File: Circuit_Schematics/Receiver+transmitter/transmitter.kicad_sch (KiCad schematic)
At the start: 21 parts, among them Q1 2N2219, Q2 2N2219, Q3 2N2219, U2 PIR, U3 PIR, U8 RF Receiver

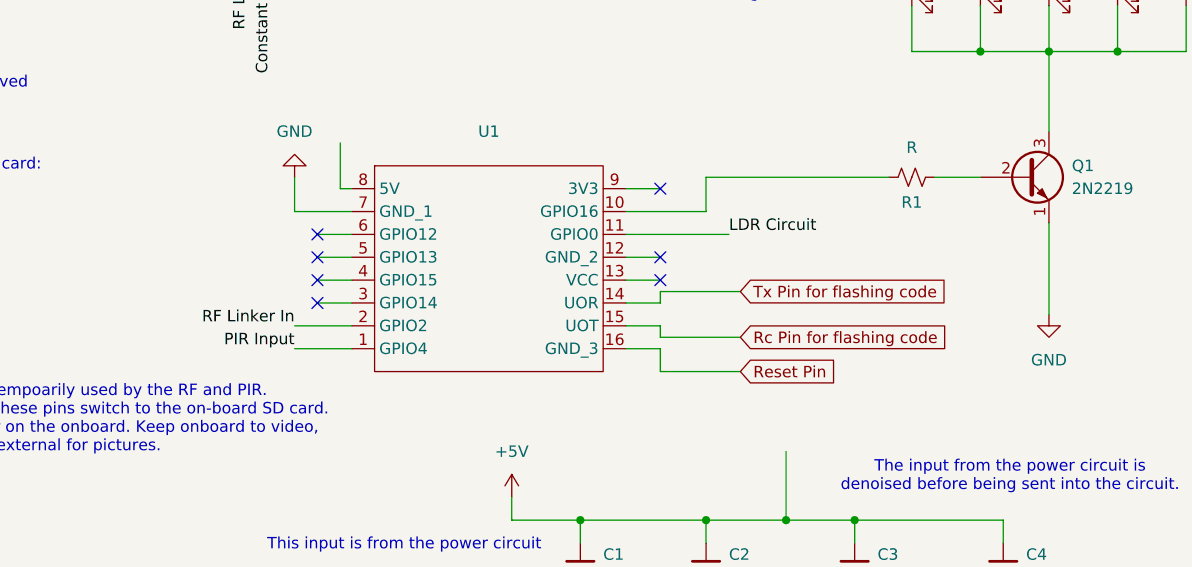
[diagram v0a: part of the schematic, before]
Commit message: Circuit schematics
Made a few additions to the circuit schematic
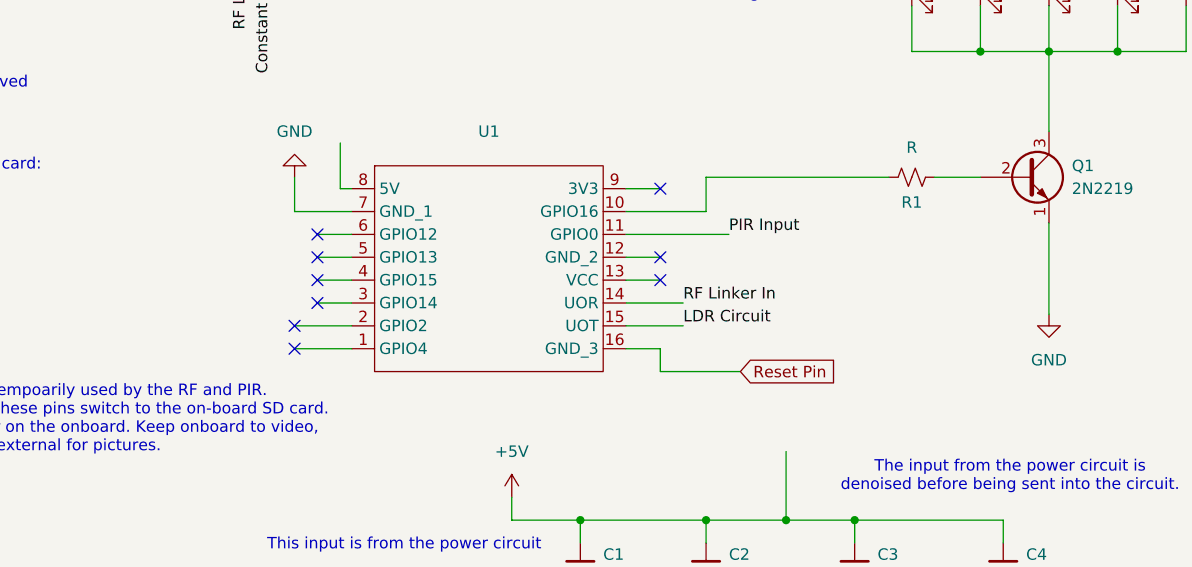
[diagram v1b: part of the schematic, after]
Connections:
- net Rc Pin for flashing code is gone; now on net LDR Circuit: U1.15 (UOT)
- net Tx Pin for flashing code is gone; now on net RF Linker In: U1.14 (UOR)
- net LDR Circuit: no longer U1.11 (GPIO0)
- net PIR Input: now also U1.11 (GPIO0); no longer U1.1 (GPIO4)
- net RF Linker In: no longer U1.2 (GPIO2)
- no-connect marks 7 -> 9
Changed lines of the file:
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@@
+	)
+	(no_connect
+		(at 76.2 91.44)
 	)
 	(no_connect
@@
 	)
 	(no_connect
+		(at 76.2 93.98)
+	)
+	(no_connect
 		(at 78.74 88.9)
 	)
@@
 	(wire
 		(pts
-			(xy 116.84 88.9) (xy 113.03 88.9)
-		)
-		(stroke
-			(width 0)
-			(type default)
-		)
-	)
-	(wire
-		(pts
 			(xy 175.26 55.88) (xy 175.26 60.96)
 		)
@@
 	(wire
 		(pts
+			(xy 113.03 91.44) (xy 119.38 91.44)
+		)
+		(stroke
+			(width 0)
+			(type default)
+		)
+	)
+	(wire
+		(pts
 			(xy 125.73 96.52) (xy 116.84 96.52)
 		)
@@
 	(wire
 		(pts
-			(xy 125.73 87.63) (xy 116.84 87.63)
-		)
-		(stroke
-			(width 0)
-			(type default)
-		)
-	)
-	(wire
-		(pts
 			(xy 116.84 96.52) (xy 116.84 93.98)
 		)
@@
 	(wire
 		(pts
-			(xy 116.84 87.63) (xy 116.84 88.9)
-		)
-		(stroke
-			(width 0)
-			(type default)
-		)
-	)
-	(wire
-		(pts
 			(xy 76.2 91.44) (xy 82.55 91.44)
 		)
@@
 	(wire
 		(pts
-			(xy 116.84 92.71) (xy 116.84 91.44)
-		)
-		(stroke
-			(width 0)
-			(type default)
-		)
-	)
-	(wire
-		(pts
 			(xy 116.84 83.82) (xy 113.03 83.82)
 		)
@@
 	(wire
 		(pts
-			(xy 125.73 92.71) (xy 116.84 92.71)
-		)
-		(stroke
-			(width 0)
-			(type default)
-		)
-	)
-	(wire
-		(pts
 			(xy 116.84 76.2) (xy 113.03 76.2)
 		)
@@
 	(wire
 		(pts
-			(xy 116.84 91.44) (xy 113.03 91.44)
-		)
-		(stroke
-			(width 0)
-			(type default)
-		)
-	)
-	(wire
-		(pts
 			(xy 175.26 48.26) (xy 175.26 39.37)
 		)
@@
 		(pts
 			(xy 160.02 60.96) (xy 167.64 60.96)
+		)
+		(stroke
+			(width 0)
+			(type default)
+		)
+	)
+	(wire
+		(pts
+			(xy 113.03 88.9) (xy 119.38 88.9)
 		)
 		(stroke
@@
 	)
 	(label "LDR Circuit"
-		(at 124.46 81.28 0)
+		(at 119.38 91.44 0)
 		(fields_autoplaced yes)
 		(effects
@@
 	)
 	(label "RF Linker In"
-		(at 76.2 91.44 180)
+		(at 119.38 88.9 0)
 		(fields_autoplaced yes)
 		(effects
@@
 				(size 1.27 1.27)
 			)
-			(justify right bottom)
+			(justify left bottom)
 		)
 	)
 	(label "PIR Input"
-		(at 76.2 93.98 180)
+		(at 124.46 81.28 0)
 		(fields_autoplaced yes)
 		(effects
@@
 				(size 1.27 1.27)
 			)
-			(justify right bottom)
-		)
-	)
-	(global_label "Tx Pin for flashing code"
-		(shape input)
-		(at 125.73 87.63 0)
-		(fields_autoplaced yes)
-		(effects
-			(font
-				(size 1.27 1.27)
-			)
-			(justify left)
-		)
-		(property "Intersheetrefs" "${INTERSHEET_REFS}"
-			(at 152.361 87.63 0)
-			(effects
-				(font
-					(size 1.27 1.27)
-				)
-				(justify left)
-				(hide yes)
-			)
-		)
-	)
-	(global_label "Rc Pin for flashing code"
-		(shape input)
-		(at 125.73 92.71 0)
-		(fields_autoplaced yes)
-		(effects
-			(font
-				(size 1.27 1.27)
-			)
-			(justify left)
-		)
-		(property "Intersheetrefs" "${INTERSHEET_REFS}"
-			(at 152.7239 92.71 0)
-			(effects
-				(font
-					(size 1.27 1.27)
-				)
-				(justify left)
-				(hide yes)
-			)
-		)
-	)
+			(justify left bottom)
+		)
+	)

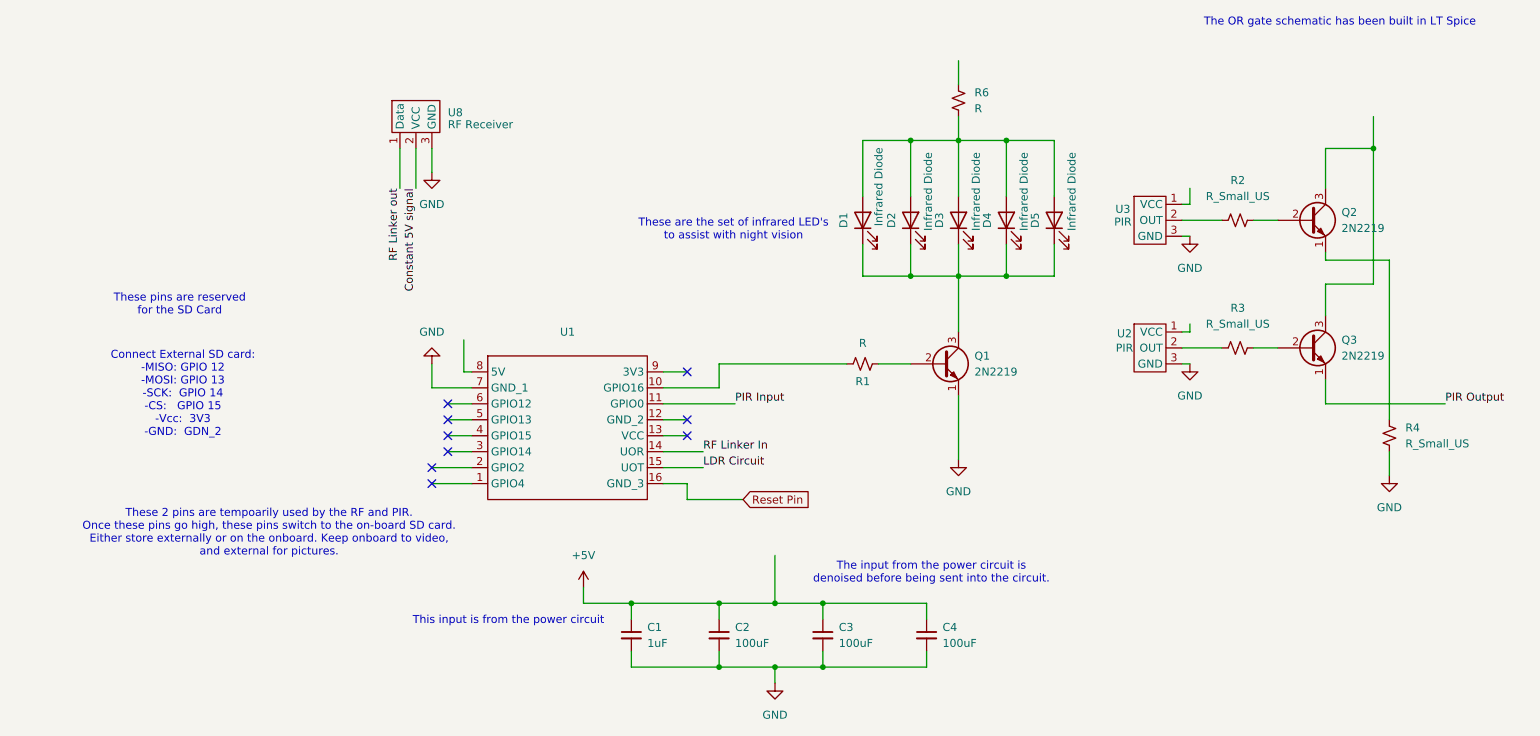
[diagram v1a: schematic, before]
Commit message: Final revision of KiCAD Docs
Edited the transmitter and receiver schematics to reflect the recent changes
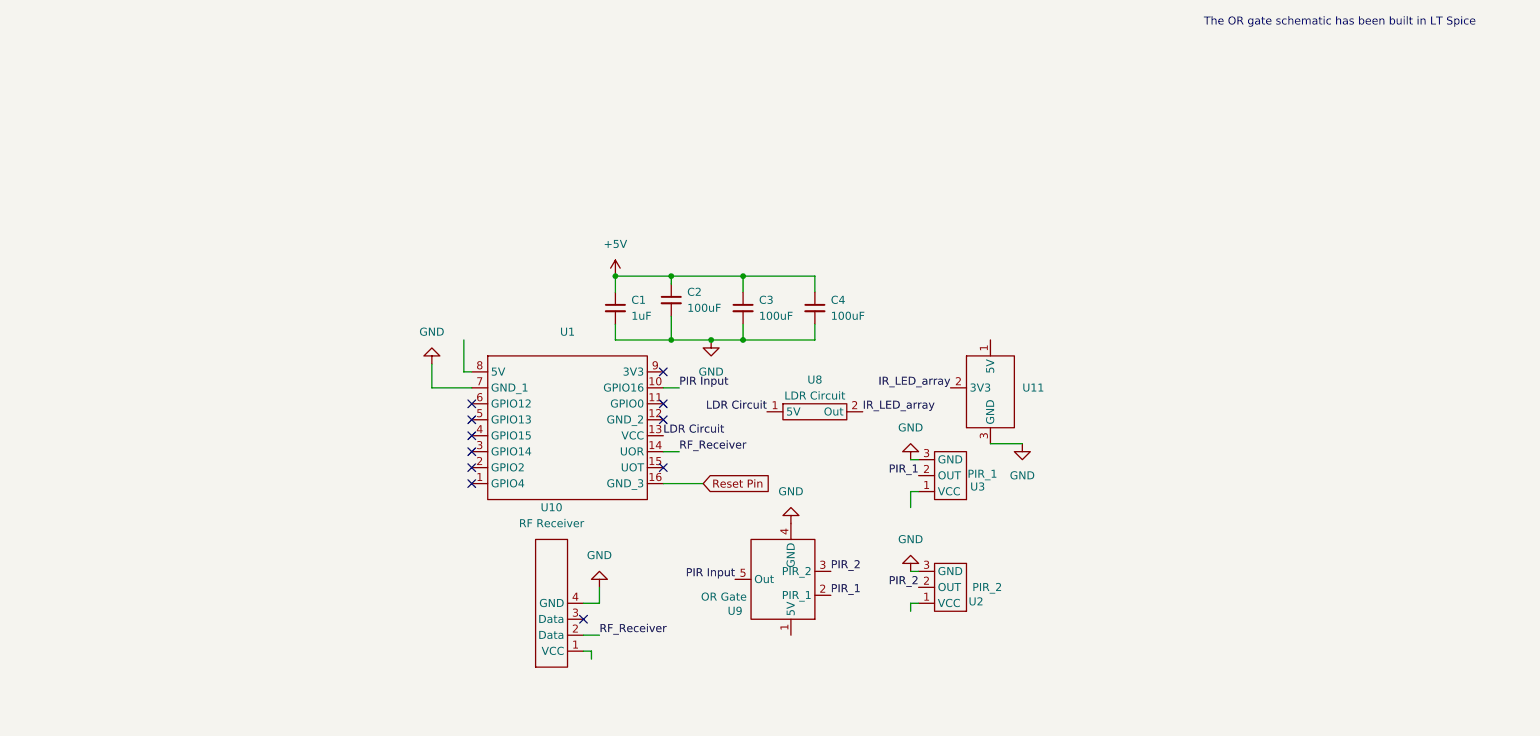
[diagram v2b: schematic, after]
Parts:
- removed D1, D2, D3, D4, D5: Infrared Diode, symbol Device:LED
- removed Q1, Q2, Q3: 2N2219, Package_TO_SOT_THT:TO-39-3, symbol Transistor_BJT:2N2219
- removed R1, R6: R, symbol Device:R_Small_US
- removed R2, R3, R4: R_Small_US, symbol Device:R_Small_US
- removed U8: RF Receiver, symbol Component:RF_Receiver
- added U10: RF Receiver, symbol Component:RF_Receiver
- added U11: ~, symbol Component:LED_Array
- added U8: LDR Circuit, symbol Component:LDR_circuit
- added U9: OR Gate, symbol Component:Comparator
- U2: value PIR -> PIR_2
- U3: value PIR -> PIR_1
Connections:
- net GND: now also U10.4 (GND), U11.3 (GND), U9.4 (GND)
- net LDR Circuit: now also U1.13 (VCC), U8.1 (5V); no longer U1.15 (UOT)
- net PIR Input: now also U1.10 (GPIO16), U9.5 (Out); no longer U1.11 (GPIO0)
- net PIR_2: now reaches U2.2 (OUT)
- net PIR_2: now also U9.3 (PIR_2)
- net PIR_1: now reaches U3.2 (OUT)
- net PIR_1: now also U9.2 (PIR_1)
- net RF Linker In renamed RF_Receiver
- net RF_Receiver: now also U10.2 (Data)
- new net IR_LED_array: U11.2 (3V3), U8.2 (Out)
- no-connect marks 9 -> 11
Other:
- note removed: "Connect External SD card: -MISO: GPIO 12 -MOSI: GPIO 13 -SCK: GPIO 14 -CS: GPIO 15 -Vcc: 3V3 -GND: GDN_2"
- note removed: "The input from the power circuit is denoised before being sent into the circuit."
- note removed: "These 2 pins are tempoarily used by the RF and PIR. Once these pins go high, these pins switch to the on-board SD card. Either store externally or on the onboard. Keep onboard to video, and external for pictures."
- note removed: "These are the set of infrared LED's to assist with night vision"
- note removed: "These pins are reserved for the SD Card"
- note removed: "This input is from the power circuit"
- moved on the sheet: C1, C2, C3, C4, U2, U3
